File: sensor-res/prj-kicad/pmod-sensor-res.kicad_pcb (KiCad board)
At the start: 2 copper layers, 50.8 x 20.3 mm, 2 parts, among them P1 PMOD

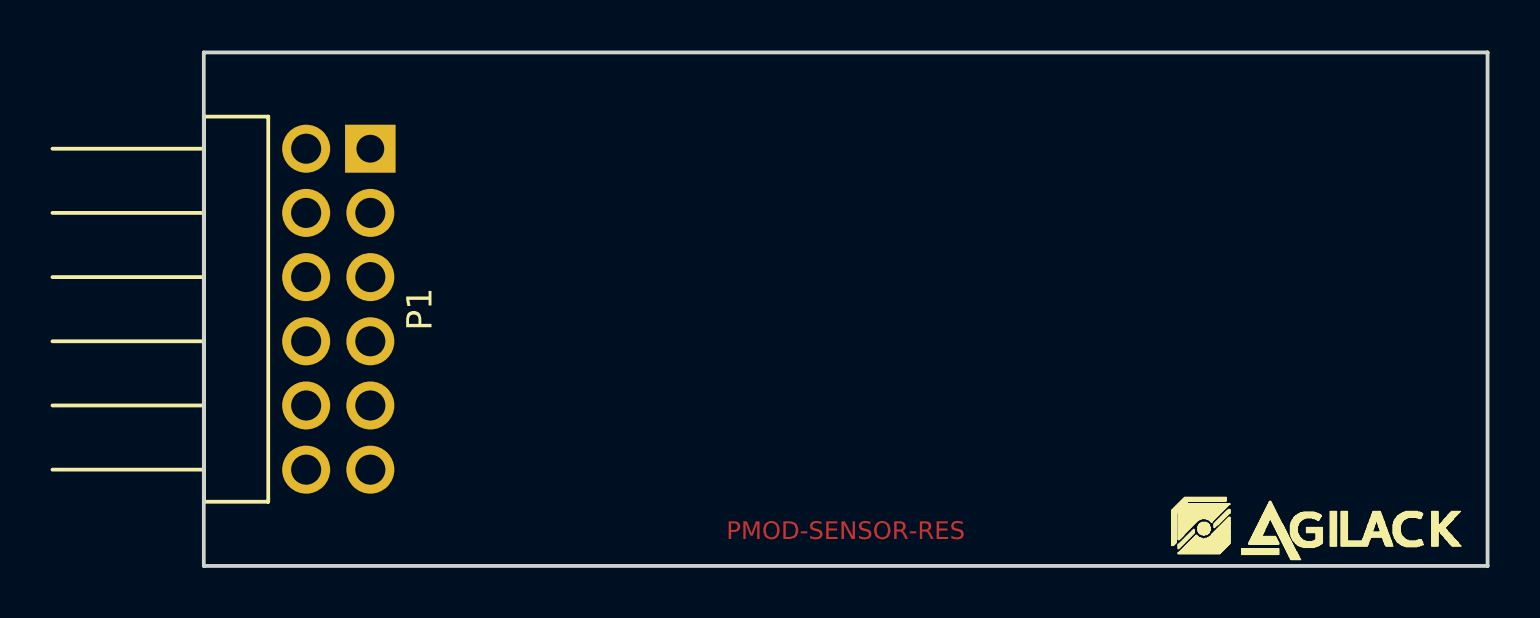
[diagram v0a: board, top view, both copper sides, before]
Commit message: SENSOR-RES: Routing is now complete
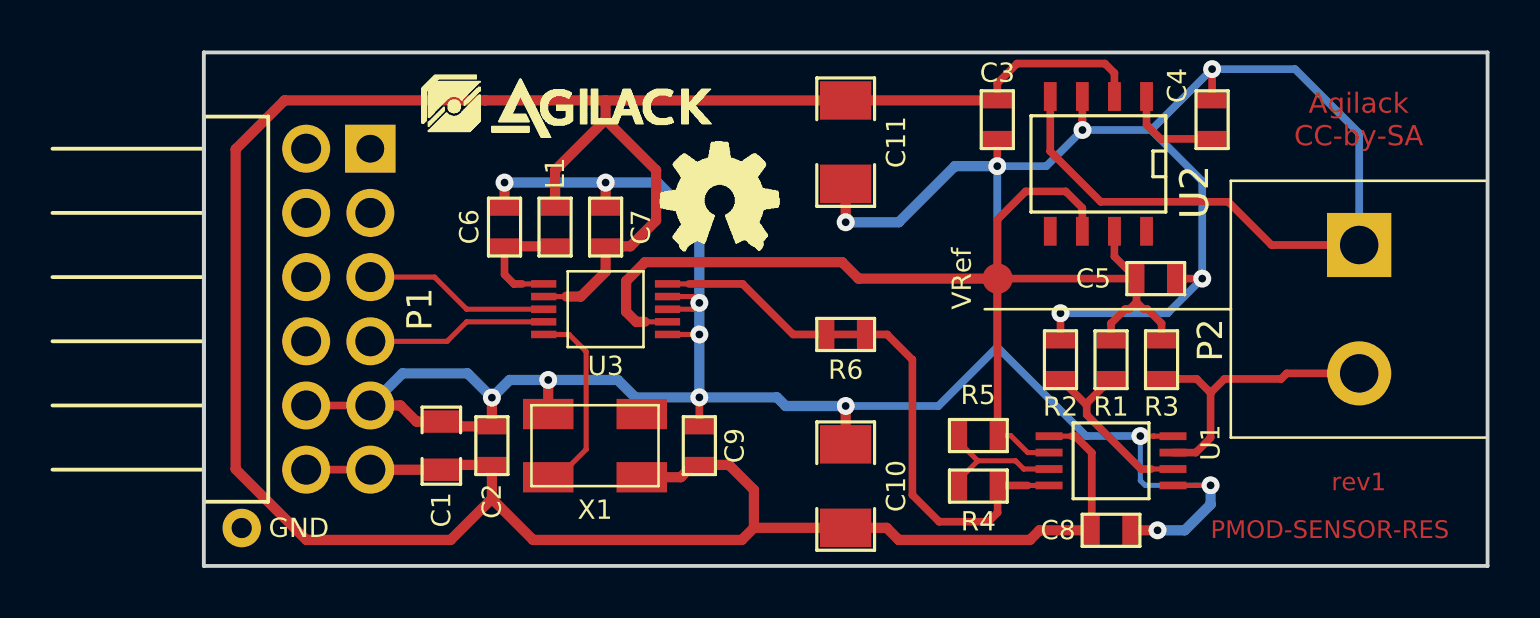
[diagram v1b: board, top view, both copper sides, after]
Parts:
- added C1: 10uF, pmod-sensor-res:SMD0805, F.Cu at (132.5, 110.4)
- added C10: 2,2uF, pmod-sensor-res:SMD1206, F.Cu at (148.5, 112.0)
- added C11: 2,2uF, pmod-sensor-res:SMD1206, F.Cu at (148.5, 98.4)
- added C2: 100nF, pmod-sensor-res:SMD0603, F.Cu at (134.5, 110.4)
- added C3: 100nF, pmod-sensor-res:SMD0603, F.Cu at (154.5, 97.5)
- added C4: 100nF, pmod-sensor-res:SMD0603, F.Cu at (163.0, 97.5)
- added C5: 1uF, pmod-sensor-res:SMD0603, F.Cu at (160.8, 103.8)
- added C6: 100nF, pmod-sensor-res:SMD0603, F.Cu at (135.0, 101.8)
- added C7: 100nF, pmod-sensor-res:SMD0603, F.Cu at (139.0, 101.8)
- added C8: 100nF, pmod-sensor-res:SMD0603, F.Cu at (159.0, 113.8)
- added C9: 100nF, pmod-sensor-res:SMD0603, F.Cu at (142.7, 110.4)
- added L1: FB100, pmod-sensor-res:SMD0603, F.Cu at (137.0, 101.8)
- added LOGO-OHW: VAL**, pmod-sensor-res:logo-ohw, F.Cu at (143.5, 100.6)
- added P2: CONN_2, pmod-sensor-res:MC000034, F.Cu at (168.8, 105.0)
- added R1: 10k, pmod-sensor-res:SMD0603, F.Cu at (159.0, 107.0)
- added R2: 100, pmod-sensor-res:SMD0603, F.Cu at (157.0, 107.0)
- added R3: 10k, pmod-sensor-res:SMD0603, F.Cu at (161.0, 107.0)
- added R4: R, pmod-sensor-res:SMD0603, F.Cu at (153.8, 112.0)
- added R5: R, pmod-sensor-res:SMD0603, F.Cu at (153.8, 110.0)
- added R6: 0, pmod-sensor-res:SMD0603, F.Cu at (148.5, 106.0)
- added TP1: CONN_1, pmod-sensor-res:TP_SMD, F.Cu at (154.5, 103.8)
- added TP2: CONN_1, pmod-sensor-res:TP, F.Cu at (124.6, 113.7)
- added U1: AD8237, pmod-sensor-res:TSSOP8, F.Cu at (159.0, 111.0)
- added U2: MAX6126, pmod-sensor-res:SOIC-8E, F.Cu at (158.5, 99.2)
- added U3: MAX11201, pmod-sensor-res:MSOP-10, F.Cu at (139.0, 105.0)
- added X1: OSC, pmod-sensor-res:Q_SMD5x3, F.Cu at (138.6, 110.4)
- moved agilack-11.5 34.1 mm to (137.9, 97.0)
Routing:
- net GND: track 0.00 -> 152.0 mm, vias 0 -> 17
- net +3.3V: track 0.00 -> 124.1 mm
- net +VSensor: track 0.00 -> 46.9 mm
- net Net-(R4-Pad2): track 0.00 -> 23.4 mm
- net /S_IN: track 0.00 -> 11.9 mm
- net MCLK: track 0.00 -> 7.79 mm
- net /S_REF: track 0.00 -> 7.59 mm
- net SPI_MISO: track 0.00 -> 7.39 mm
- net SPI_SCK: track 0.00 -> 7.18 mm
- net Net-(R4-Pad1): track 0.00 -> 5.57 mm
- net Net-(C6-Pad1): track 0.00 -> 4.82 mm
- net Net-(C4-Pad1): track 0.00 -> 3.95 mm
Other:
- board text added: "Agilack CC-by-SA"
- board text added: "GND"
- board text added: "VRef"
- board text added: "rev1"
